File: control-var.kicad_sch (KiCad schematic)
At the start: 44 parts, among them U28001 OPA2810, U28002 OPA2810, U28003 OPA2810

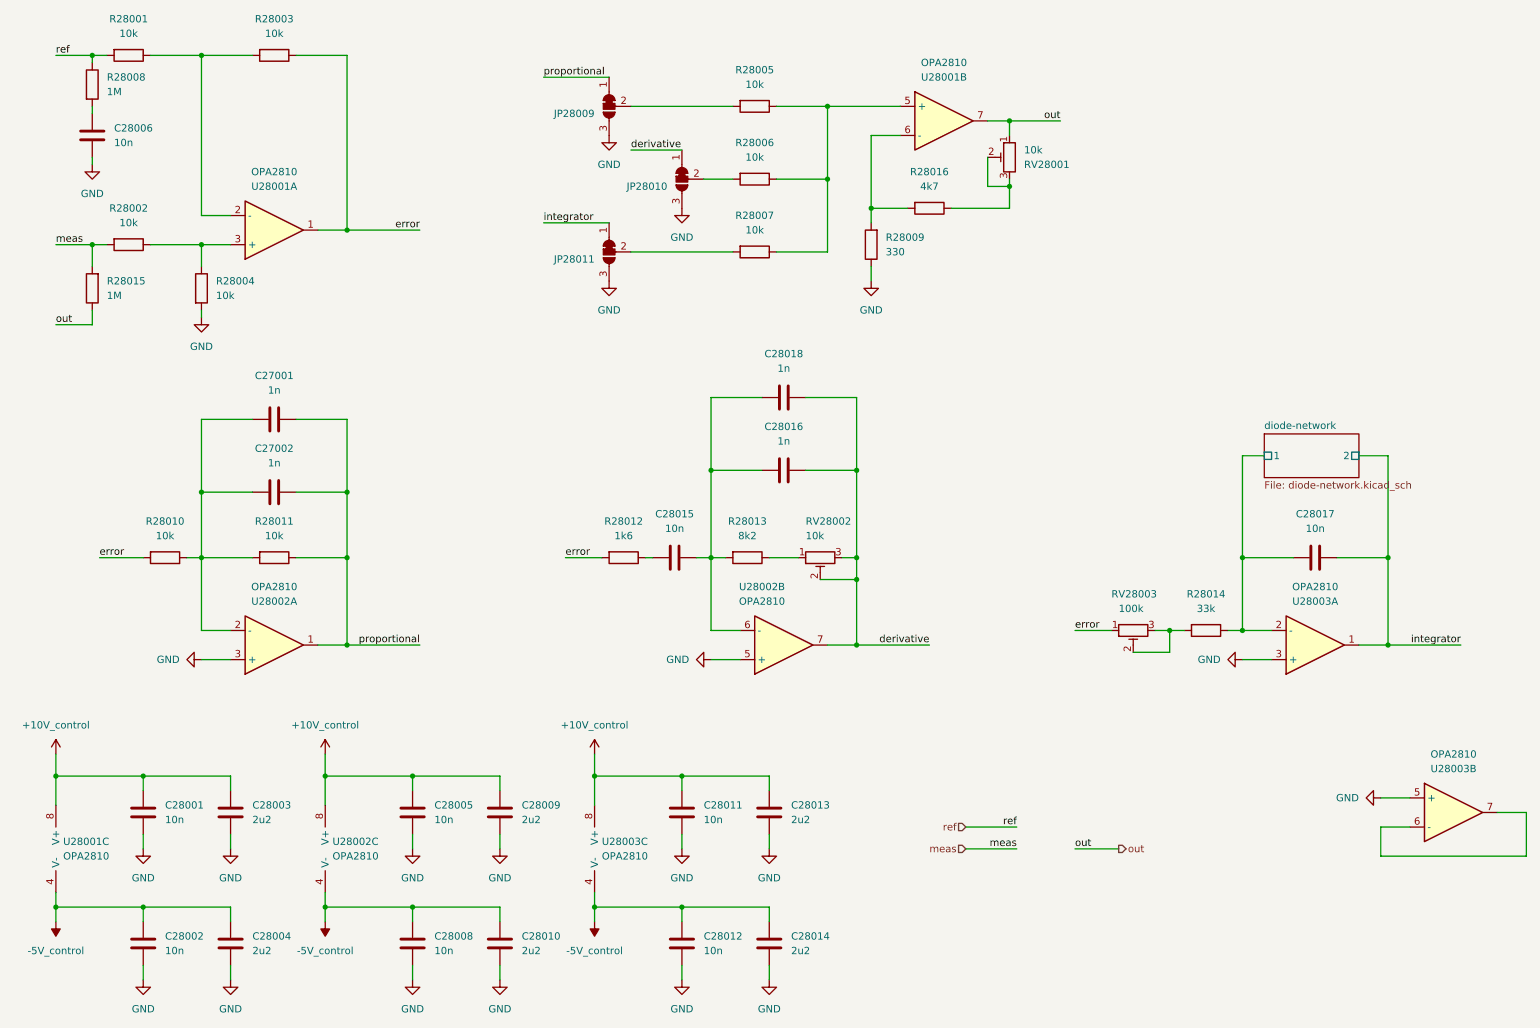
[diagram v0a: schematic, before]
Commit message: add pss 3dmodels and testpoints
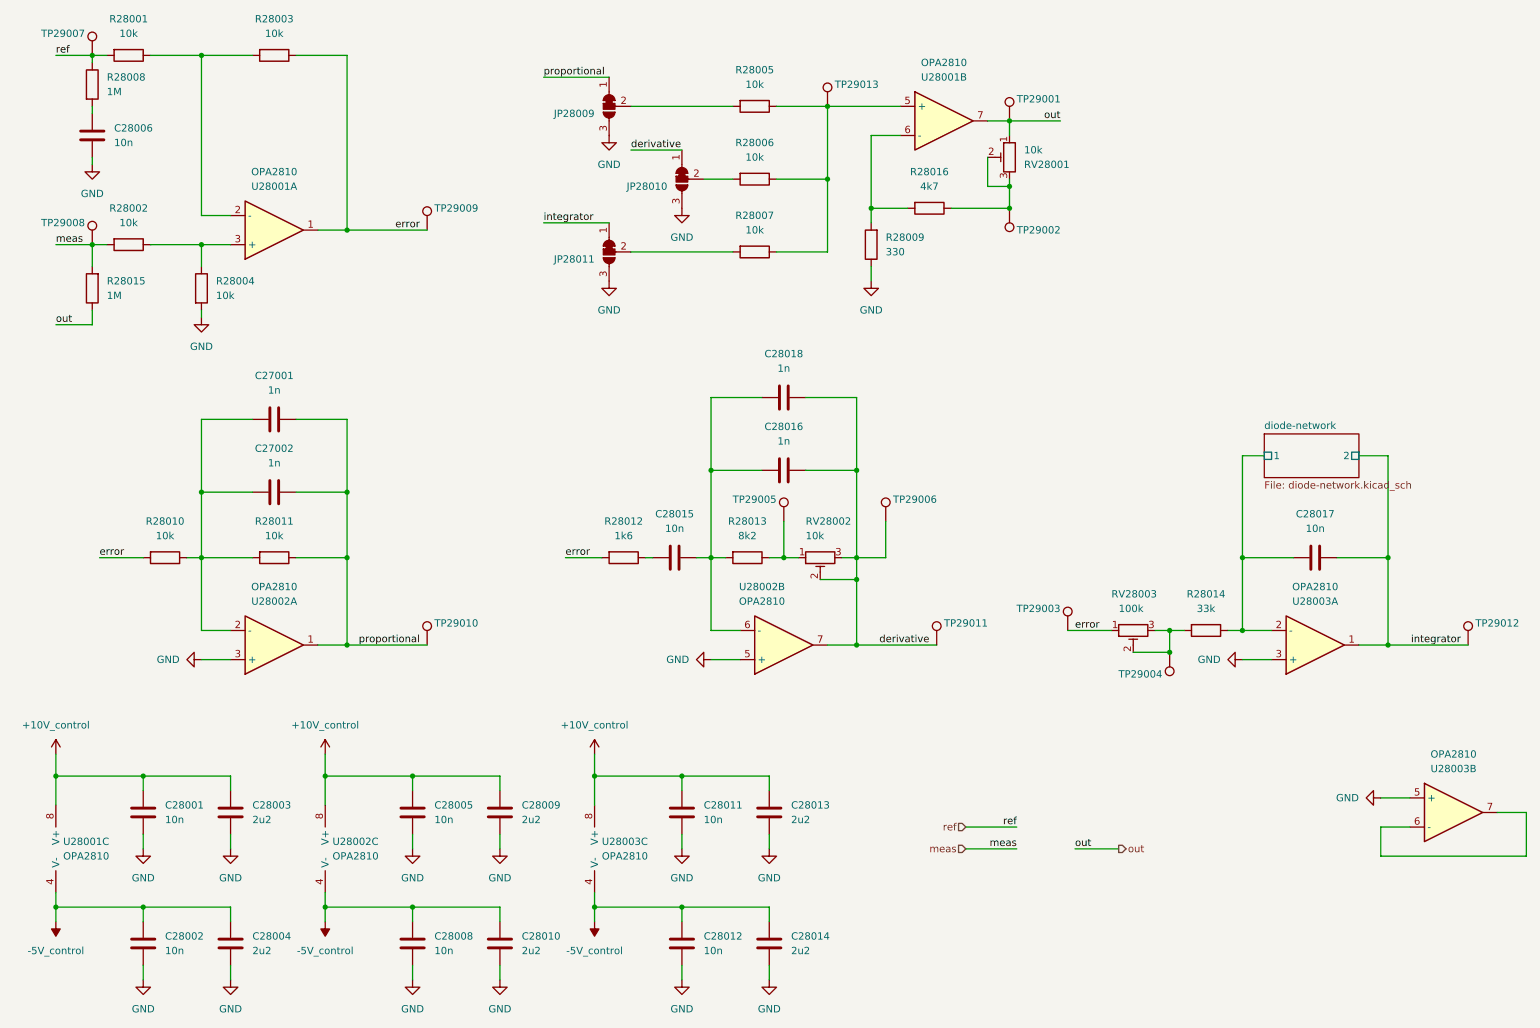
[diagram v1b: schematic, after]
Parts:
- added TP29001, TP29002, TP29003, TP29004, TP29005, TP29006, TP29007, TP29008, TP29009, TP29010, TP29011, TP29012, TP29013: ~, pss:TP_0805_2012Metric, symbol Connector:TestPoint
- JP28009, JP28010, JP28011: footprint (none) -> pss:SolderJumper-3_P1.3mm_Bridged12-Soldermask-Paste_RoundedPad1.0x1.5mm
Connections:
- net derivative: now also TP29006.1, TP29011.1
- net error: now also TP29003.1, TP29009.1
- net integrator: now also TP29012.1
- net meas: now also TP29008.1
- net out: now also TP29001.1
- net proportional: now also TP29010.1
- net ref: now also TP29007.1
- net at R28014.2, RV28003.2, RV28003.3: now also TP29004.1
- net at R28005.1, R28006.1, R28007.1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: now also TP29013.1
- net at R28013.1, RV28002.1: now also TP29005.1
- net at R28016.1, RV28001.2, RV28001.3: now also TP29002.1

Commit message: edit pss reannotate entire schematic
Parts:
- R28009: MPN RC1210FR-07330RL -> RC1210FR-07330RL

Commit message: edit pss symbol library: export all schematic symbols to library 'pss' and update symbol link
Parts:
- JP28009, JP28010, JP28011: symbol Jumper:SolderJumper_3_Bridged12 -> pss:SolderJumper_3_Bridged12
- RV28001, RV28002, RV28003: symbol Device:R_Potentiometer_Trim -> pss:R_Potentiometer_Trim
- TP29001, TP29002, TP29003, TP29004, TP29005, TP29006, TP29007, TP29008, TP29009, TP29010, TP29011, TP29012, TP29013: symbol Connector:TestPoint -> pss:TestPoint
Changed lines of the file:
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@@
 	)
 	(symbol
-		(lib_id "Device:R_Potentiometer_Trim")
+		(lib_id "pss:R_Potentiometer_Trim")
 		(at 213.36 124.46 90)
 		(mirror x)
@@
 	)
 	(symbol
-		(lib_id "Connector:TestPoint")
+		(lib_id "pss:TestPoint")
 		(at 31.75 24.13 0)
 		(mirror y)
@@
 	)
 	(symbol
-		(lib_id "Jumper:SolderJumper_3_Bridged12")
+		(lib_id "pss:SolderJumper_3_Bridged12")
 		(at 121.92 33.02 90)
 		(mirror x)
@@
 	)
 	(symbol
-		(lib_id "Connector:TestPoint")
+		(lib_id "pss:TestPoint")
 		(at 152.4 105.41 0)
 		(mirror y)
@@
 	)
 	(symbol
-		(lib_id "Connector:TestPoint")
+		(lib_id "pss:TestPoint")
 		(at 191.77 50.8 0)
 		(mirror x)
@@
 	)
 	(symbol
-		(lib_id "Connector:TestPoint")
+		(lib_id "pss:TestPoint")
 		(at 179.07 127 0)
 		(unit 1)
@@
 	)
 	(symbol
-		(lib_id "Connector:TestPoint")
+		(lib_id "pss:TestPoint")
 		(at 31.75 57.15 0)
 		(mirror y)
@@
 	)
 	(symbol
-		(lib_id "Connector:TestPoint")
+		(lib_id "pss:TestPoint")
 		(at 90.17 127 0)
 		(unit 1)
@@
 	)
 	(symbol
-		(lib_id "Device:R_Potentiometer_Trim")
+		(lib_id "pss:R_Potentiometer_Trim")
 		(at 158.75 111.76 90)
 		(mirror x)
@@
 	)
 	(symbol
-		(lib_id "Connector:TestPoint")
+		(lib_id "pss:TestPoint")
 		(at 191.77 35.56 0)
 		(unit 1)
@@
 	)
 	(symbol
-		(lib_id "Jumper:SolderJumper_3_Bridged12")
+		(lib_id "pss:SolderJumper_3_Bridged12")
 		(at 134.62 45.72 90)
 		(mirror x)
@@
 	)
 	(symbol
-		(lib_id "Connector:TestPoint")
+		(lib_id "pss:TestPoint")
 		(at 201.93 124.46 0)
 		(mirror y)
@@
 	)
 	(symbol
-		(lib_id "Connector:TestPoint")
+		(lib_id "pss:TestPoint")
 		(at 170.18 105.41 0)
 		(unit 1)
@@
 	)
 	(symbol
-		(lib_id "Connector:TestPoint")
+		(lib_id "pss:TestPoint")
 		(at 90.17 54.61 0)
 		(unit 1)
@@
 	)
 	(symbol
-		(lib_id "Connector:TestPoint")
+		(lib_id "pss:TestPoint")
 		(at 271.78 127 0)
 		(unit 1)
@@
 	)
 	(symbol
-		(lib_id "Connector:TestPoint")
+		(lib_id "pss:TestPoint")
 		(at 160.02 33.02 0)
 		(unit 1)
@@
 	)
 	(symbol
-		(lib_id "Jumper:SolderJumper_3_Bridged12")
+		(lib_id "pss:SolderJumper_3_Bridged12")
 		(at 121.92 58.42 90)
 		(mirror x)
@@
 	)
 	(symbol
-		(lib_id "Connector:TestPoint")
+		(lib_id "pss:TestPoint")
 		(at 219.71 128.27 180)
 		(unit 1)
@@
 	)
 	(symbol
-		(lib_id "Device:R_Potentiometer_Trim")
+		(lib_id "pss:R_Potentiometer_Trim")
 		(at 191.77 41.91 0)
 		(mirror y)

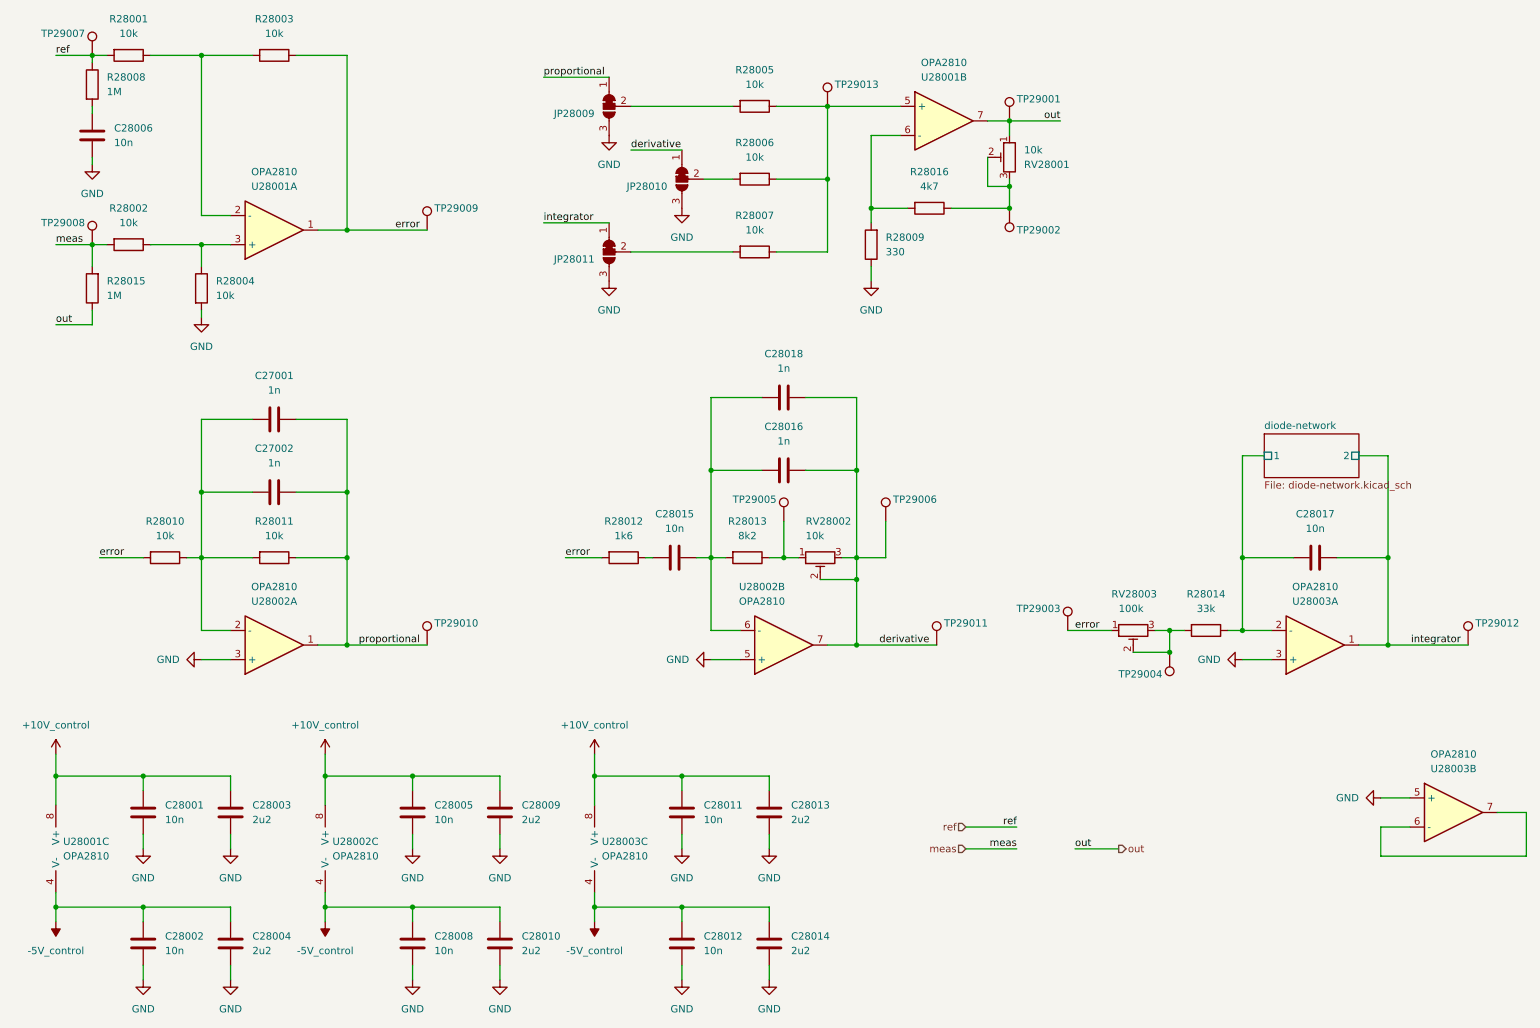
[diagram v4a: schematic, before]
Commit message: edit pss footprint library: export all footprints to library 'pss' and update footprint links
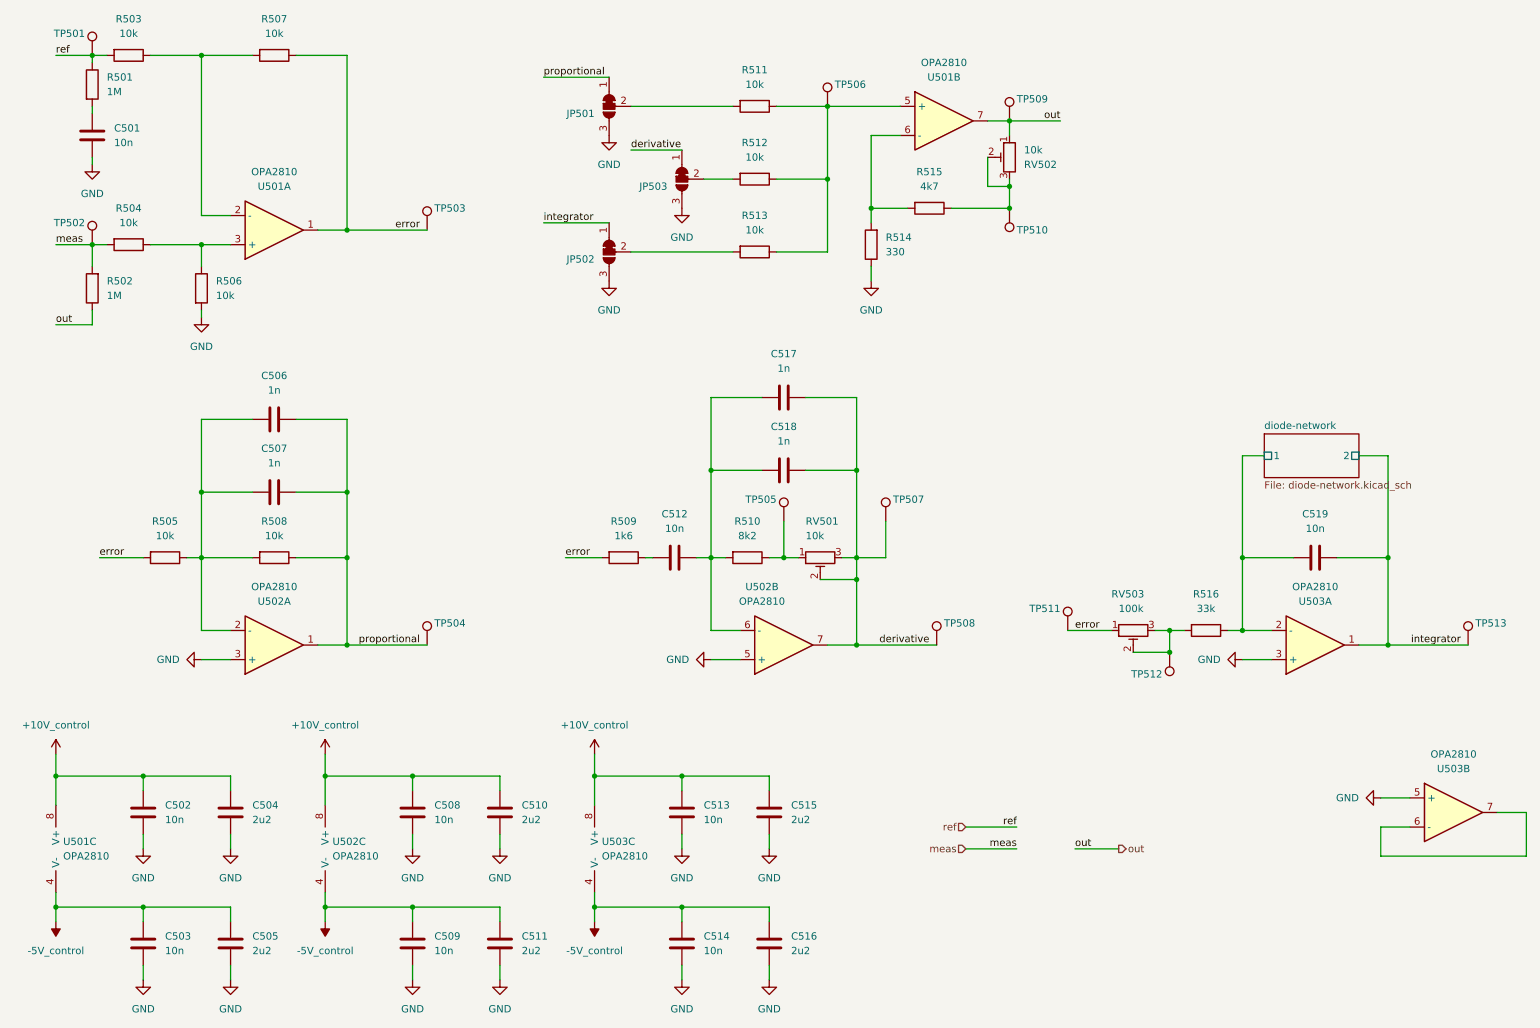
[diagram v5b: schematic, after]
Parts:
- C501: renamed from C28006; footprint Capacitor_SMD:C_0805_2012Metric_Pad1.18x1.45mm_HandSolder -> pss:C_0805_2012Metric_Pad1.18x1.45mm_HandSolder
- C502: renamed from C28001; footprint Capacitor_SMD:C_0805_2012Metric_Pad1.18x1.45mm_HandSolder -> pss:C_0805_2012Metric_Pad1.18x1.45mm_HandSolder
- C503: renamed from C28002; footprint Capacitor_SMD:C_0805_2012Metric_Pad1.18x1.45mm_HandSolder -> pss:C_0805_2012Metric_Pad1.18x1.45mm_HandSolder
- C504: renamed from C28003; footprint Capacitor_SMD:C_0805_2012Metric_Pad1.18x1.45mm_HandSolder -> pss:C_0805_2012Metric_Pad1.18x1.45mm_HandSolder
- C505: renamed from C28004; footprint Capacitor_SMD:C_0805_2012Metric_Pad1.18x1.45mm_HandSolder -> pss:C_0805_2012Metric_Pad1.18x1.45mm_HandSolder
- C506: renamed from C27001; footprint Capacitor_SMD:C_0805_2012Metric_Pad1.18x1.45mm_HandSolder -> pss:C_0805_2012Metric_Pad1.18x1.45mm_HandSolder
- C507: renamed from C27002; footprint Capacitor_SMD:C_0805_2012Metric_Pad1.18x1.45mm_HandSolder -> pss:C_0805_2012Metric_Pad1.18x1.45mm_HandSolder
- C508: renamed from C28005; footprint Capacitor_SMD:C_0805_2012Metric_Pad1.18x1.45mm_HandSolder -> pss:C_0805_2012Metric_Pad1.18x1.45mm_HandSolder
- C509: renamed from C28008; footprint Capacitor_SMD:C_0805_2012Metric_Pad1.18x1.45mm_HandSolder -> pss:C_0805_2012Metric_Pad1.18x1.45mm_HandSolder
- C510: renamed from C28009; footprint Capacitor_SMD:C_0805_2012Metric_Pad1.18x1.45mm_HandSolder -> pss:C_0805_2012Metric_Pad1.18x1.45mm_HandSolder
- C511: renamed from C28010; footprint Capacitor_SMD:C_0805_2012Metric_Pad1.18x1.45mm_HandSolder -> pss:C_0805_2012Metric_Pad1.18x1.45mm_HandSolder
- C512: renamed from C28015; footprint Capacitor_SMD:C_0805_2012Metric_Pad1.18x1.45mm_HandSolder -> pss:C_0805_2012Metric_Pad1.18x1.45mm_HandSolder
- C513: renamed from C28011; footprint Capacitor_SMD:C_0805_2012Metric_Pad1.18x1.45mm_HandSolder -> pss:C_0805_2012Metric_Pad1.18x1.45mm_HandSolder
- C514: renamed from C28012; footprint Capacitor_SMD:C_0805_2012Metric_Pad1.18x1.45mm_HandSolder -> pss:C_0805_2012Metric_Pad1.18x1.45mm_HandSolder
- C515: renamed from C28013; footprint Capacitor_SMD:C_0805_2012Metric_Pad1.18x1.45mm_HandSolder -> pss:C_0805_2012Metric_Pad1.18x1.45mm_HandSolder
- C516: renamed from C28014; footprint Capacitor_SMD:C_0805_2012Metric_Pad1.18x1.45mm_HandSolder -> pss:C_0805_2012Metric_Pad1.18x1.45mm_HandSolder
- C517: renamed from C28018; footprint Capacitor_SMD:C_0805_2012Metric_Pad1.18x1.45mm_HandSolder -> pss:C_0805_2012Metric_Pad1.18x1.45mm_HandSolder
- C518: renamed from C28016; footprint Capacitor_SMD:C_0805_2012Metric_Pad1.18x1.45mm_HandSolder -> pss:C_0805_2012Metric_Pad1.18x1.45mm_HandSolder
- C519: renamed from C28017; footprint Capacitor_SMD:C_0805_2012Metric_Pad1.18x1.45mm_HandSolder -> pss:C_0805_2012Metric_Pad1.18x1.45mm_HandSolder
- R501: renamed from R28008; footprint Resistor_SMD:R_1210_3225Metric_Pad1.30x2.65mm_HandSolder -> pss:R_1210_3225Metric_Pad1.30x2.65mm_HandSolder
- R502: renamed from R28015; footprint Resistor_SMD:R_1210_3225Metric_Pad1.30x2.65mm_HandSolder -> pss:R_1210_3225Metric_Pad1.30x2.65mm_HandSolder
- R503: renamed from R28001; footprint Resistor_SMD:R_1210_3225Metric_Pad1.30x2.65mm_HandSolder -> pss:R_1210_3225Metric_Pad1.30x2.65mm_HandSolder
- R504: renamed from R28002; footprint Resistor_SMD:R_1210_3225Metric_Pad1.30x2.65mm_HandSolder -> pss:R_1210_3225Metric_Pad1.30x2.65mm_HandSolder
- R505: renamed from R28010; footprint Resistor_SMD:R_1210_3225Metric_Pad1.30x2.65mm_HandSolder -> pss:R_1210_3225Metric_Pad1.30x2.65mm_HandSolder
- R506: renamed from R28004; footprint Resistor_SMD:R_1210_3225Metric_Pad1.30x2.65mm_HandSolder -> pss:R_1210_3225Metric_Pad1.30x2.65mm_HandSolder
- R507: renamed from R28003; footprint Resistor_SMD:R_1210_3225Metric_Pad1.30x2.65mm_HandSolder -> pss:R_1210_3225Metric_Pad1.30x2.65mm_HandSolder
- R508: renamed from R28011; footprint Resistor_SMD:R_1210_3225Metric_Pad1.30x2.65mm_HandSolder -> pss:R_1210_3225Metric_Pad1.30x2.65mm_HandSolder
- R509: renamed from R28012; footprint Resistor_SMD:R_1210_3225Metric_Pad1.30x2.65mm_HandSolder -> pss:R_1210_3225Metric_Pad1.30x2.65mm_HandSolder
- R510: renamed from R28013; footprint Resistor_SMD:R_1210_3225Metric_Pad1.30x2.65mm_HandSolder -> pss:R_1210_3225Metric_Pad1.30x2.65mm_HandSolder
- R511: renamed from R28005; footprint Resistor_SMD:R_1210_3225Metric_Pad1.30x2.65mm_HandSolder -> pss:R_1210_3225Metric_Pad1.30x2.65mm_HandSolder
- R512: renamed from R28006; footprint Resistor_SMD:R_1210_3225Metric_Pad1.30x2.65mm_HandSolder -> pss:R_1210_3225Metric_Pad1.30x2.65mm_HandSolder
- R513: renamed from R28007; footprint Resistor_SMD:R_1210_3225Metric_Pad1.30x2.65mm_HandSolder -> pss:R_1210_3225Metric_Pad1.30x2.65mm_HandSolder
- R514: renamed from R28009; footprint Resistor_SMD:R_1210_3225Metric_Pad1.30x2.65mm_HandSolder -> pss:R_1210_3225Metric_Pad1.30x2.65mm_HandSolder
- R515: renamed from R28016; footprint Resistor_SMD:R_1210_3225Metric_Pad1.30x2.65mm_HandSolder -> pss:R_1210_3225Metric_Pad1.30x2.65mm_HandSolder
- R516: renamed from R28014; footprint Resistor_SMD:R_1210_3225Metric_Pad1.30x2.65mm_HandSolder -> pss:R_1210_3225Metric_Pad1.30x2.65mm_HandSolder
- U501: renamed from U28001; footprint Package_SO:SOIC-8_3.9x4.9mm_P1.27mm -> pss:SOIC-8_3.9x4.9mm_P1.27mm
- U502: renamed from U28002; footprint Package_SO:SOIC-8_3.9x4.9mm_P1.27mm -> pss:SOIC-8_3.9x4.9mm_P1.27mm
- U503: renamed from U28003; footprint Package_SO:SOIC-8_3.9x4.9mm_P1.27mm -> pss:SOIC-8_3.9x4.9mm_P1.27mm
- renumbered JP28009 to JP501, JP28011 to JP502, JP28010 to JP503, RV28002 to RV501, RV28001 to RV502, RV28003 to RV503, TP29007 to TP501, TP29008 to TP502, TP29009 to TP503, TP29010 to TP504, TP29005 to TP505, TP29013 to TP506, TP29006 to TP507, TP29011 to TP508, TP29001 to TP509, TP29002 to TP510, TP29003 to TP511, TP29004 to TP512, TP29012 to TP513
